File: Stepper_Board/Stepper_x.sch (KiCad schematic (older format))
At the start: 14 parts

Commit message: Testsoftware for ImageProcessing in c programmiert
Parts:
- removed C?: 22n 50V, Capacitor_SMD:C_0603_1608Metric, symbol Device:C_Small
- removed C? (x3): 100n 50V, Capacitor_SMD:C_0603_1608Metric, symbol Device:C_Small
- removed C?: 100u 35V, Capacitor_THT:CP_Radial_D6.3mm_P2.50mm, symbol Device:CP_Small
- removed R?: 0.1R 0.5W, Resistor_SMD:R_1210_3225Metric, symbol Device:R_Small
- added C201, C205, C206: 100n 50V, Capacitor_SMD:C_0603_1608Metric, symbol Device:C_Small
- added C204: 22n 50V, Capacitor_SMD:C_0603_1608Metric, symbol Device:C_Small
- added C208: 100u 35V, Capacitor_THT:CP_Radial_D6.3mm_P2.50mm, symbol Device:CP_Small
- added R203: 0.22R 0.5W, Resistor_SMD:R_1210_3225Metric, symbol Device:R_Small
- R202: renamed from R?; value 0.1R 0.5W -> 0.22R 0.5W; LCSC C270892 -> C159293
- U201: renamed from U?; symbol Pick_n_Place:TMC2226 -> StepperBoard-rescue:TMC2226-Pick_n_Place
- gave numbers to parts that had none: 6
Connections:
- net labels added: CUR_CONTROL, DIAG, DIR, EN, INDEX, OA1, OA2, OB1, OB2, STEP
- net labels removed: CUR_CONTROL_X, DIAG_X, DIR_X, EN_X, INDEX_X, OA1_X, OA2_X, OB1_X, OB2_X, STEP_X
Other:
- note added: "100mOhm C270892"
- note added: "960mA"
- note removed: "1920mA"

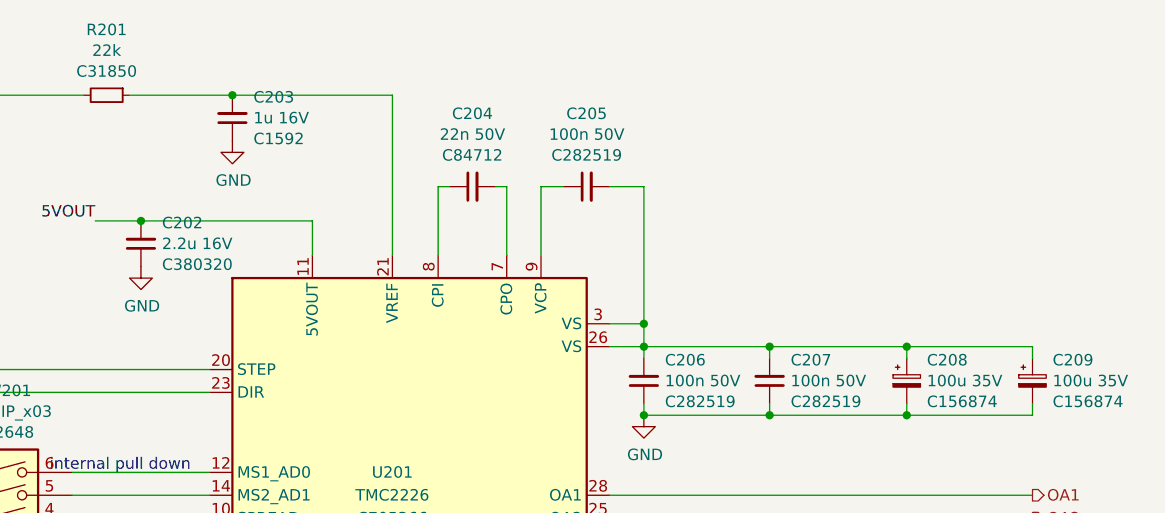
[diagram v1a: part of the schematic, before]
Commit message: STM32F401 für motoransteuerung gewählt. TODO: motoransteuerung und leistungsteil trennen, damit für schnelle fehlerbehebung modul getauscht werden kann
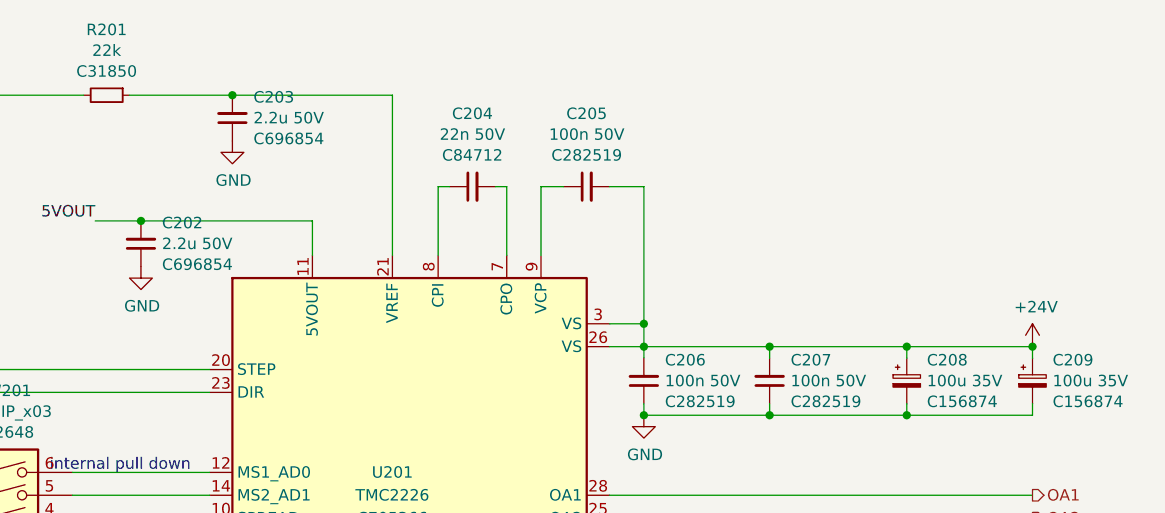
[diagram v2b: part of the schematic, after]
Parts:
- C202: value 2.2u 16V -> 2.2u 50V; footprint Capacitor_SMD:C_0603_1608Metric -> Capacitor_SMD:C_1210_3225Metric; LCSC C380320 -> C696854
- C203: value 1u 16V -> 2.2u 50V; footprint Capacitor_SMD:C_0603_1608Metric -> Capacitor_SMD:C_1210_3225Metric; LCSC C1592 -> C696854
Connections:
- net +24V: now reaches C205.2, C206.2, C207.2, C208.1, C209.1, U201.26 (VS), U201.3 (VS)
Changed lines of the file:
@@
 AR Path="/5FCAC453/5FBD37D6" Ref="C?"  Part="1"
 F 0 "C202" H 5458 1509 50  0000 R CNN
-F 1 "2.2u 16V" H 5458 1600 50  0000 R CNN
-F 2 "Capacitor_SMD:C_0603_1608Metric" H 5550 1600 50  0001 C CNN
+F 1 "2.2u 50V" H 5458 1600 50  0000 R CNN
+F 2 "Capacitor_SMD:C_1210_3225Metric" H 5550 1600 50  0001 C CNN
 F 3 "~" H 5550 1600 50  0001 C CNN
-F 4 "C380320 " H 5458 1691 50  0000 R CNN "LCSC"
+F 4 " C696854 " H 5458 1691 50  0000 R CNN "LCSC"
 	1    5550 1600
 	-1   0    0    1
@@
 AR Path="/5FCAC453/5FBDC148" Ref="C?"  Part="1"
 F 0 "C203" H 5858 959 50  0000 R CNN
-F 1 "1u 16V" H 5858 1050 50  0000 R CNN
-F 2 "Capacitor_SMD:C_0603_1608Metric" H 5950 1050 50  0001 C CNN
+F 1 "2.2u 50V" H 5858 1050 50  0000 R CNN
+F 2 "Capacitor_SMD:C_1210_3225Metric" H 5950 1050 50  0001 C CNN
 F 3 "~" H 5950 1050 50  0001 C CNN
-F 4 "C1592" H 5858 1141 50  0000 R CNN "LCSC"
+F 4 " C696854 " H 5858 1141 50  0000 R CNN "LCSC"
 	1    5950 1050
 	-1   0    0    1
@@
 Text Notes 7700 4100 0    50   ~ 0
 100mOhm C270892
+$Comp
+L power:+24V #PWR0201
+U 1 1 6004F04A
+P 9450 2050
+F 0 "#PWR0201" H 9450 1900 50  0001 C CNN
+F 1 "+24V" H 9465 2223 50  0000 C CNN
+F 2 "" H 9450 2050 50  0001 C CNN
+F 3 "" H 9450 2050 50  0001 C CNN
+	1    9450 2050
+	1    0    0    -1
+$EndComp
+Connection ~ 9450 2050
 $EndSCHEMATC
